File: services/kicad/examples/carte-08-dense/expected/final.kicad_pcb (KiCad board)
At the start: 2 copper layers, 57.3 x 44 mm, 56 parts, among them J1 IN_5V, J10 IO0, J11 IO1, J12 IO2, J13 IO3, J14 IO4, J2 SWD, U1 STM32F103C8T6, U2 AMS1117-3.3

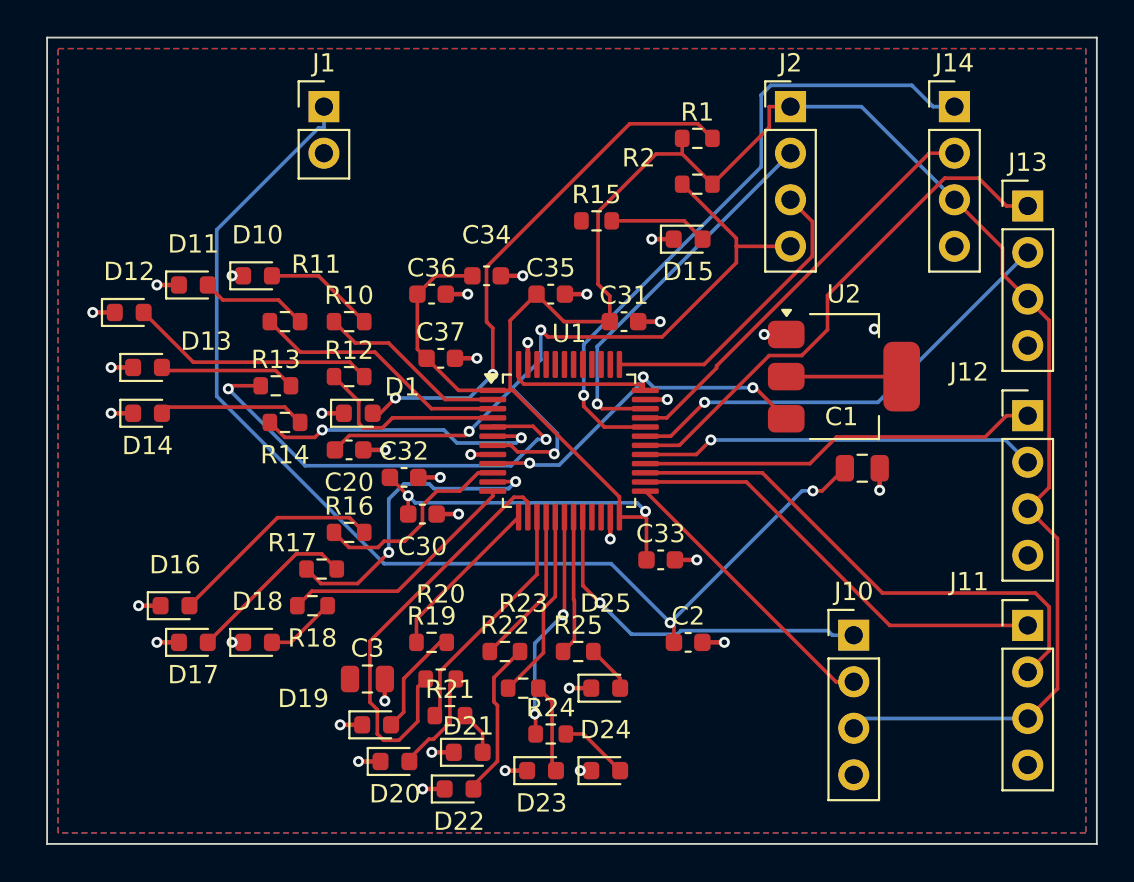
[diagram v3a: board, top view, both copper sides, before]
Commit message: fix(banc): le banc route comme la production — plafond 8, budget du client
D-2026-09-24-f. run_pipeline.py prenait 2 couches et 1800 s par défaut, et
carte-07 écrivait 2 en dur : dix cartes sur quinze ne pouvaient jamais
escalader, et la règle « toute connexion manquante fait monter » était
inerte dans le banc. Mesuré sur carte-07 : 97 %, seule la masse manquante,
« le palier suivant sera tenté »… puis retour à 2 couches.

Plafond par défaut 8 (client Pro Max), budget min(600 + 300 x plafond, 3600)
comme routingSearchBudgetS côté client. En production, rien ne change : le
plafond reste celui du plan.

Livraisons du jour, toutes vérifiées par kicad-cli et contre le schéma
(0 erreur bloquante, 0 connexion manquante, 0 court-circuit) :
carte-04, 05, 06, 08 (campagne de l'après-midi) et carte-09, 10 (4 couches).
Les boards versionnés de ces cartes court-circuitaient des nets du schéma.

Correction de ma propre erreur dans la doc : carte-07 n'avait jamais
escaladé ; les lignes « palier 4 et 6 » du journal étaient celles de
carte-08, démarrée la même minute.

Co-Authored-By: Claude Opus 5.5 <noreply@anthropic.com>
Claude-Session: https://claude.ai/code/session_01TnMqm4La2CxQHHB5K8aSSV
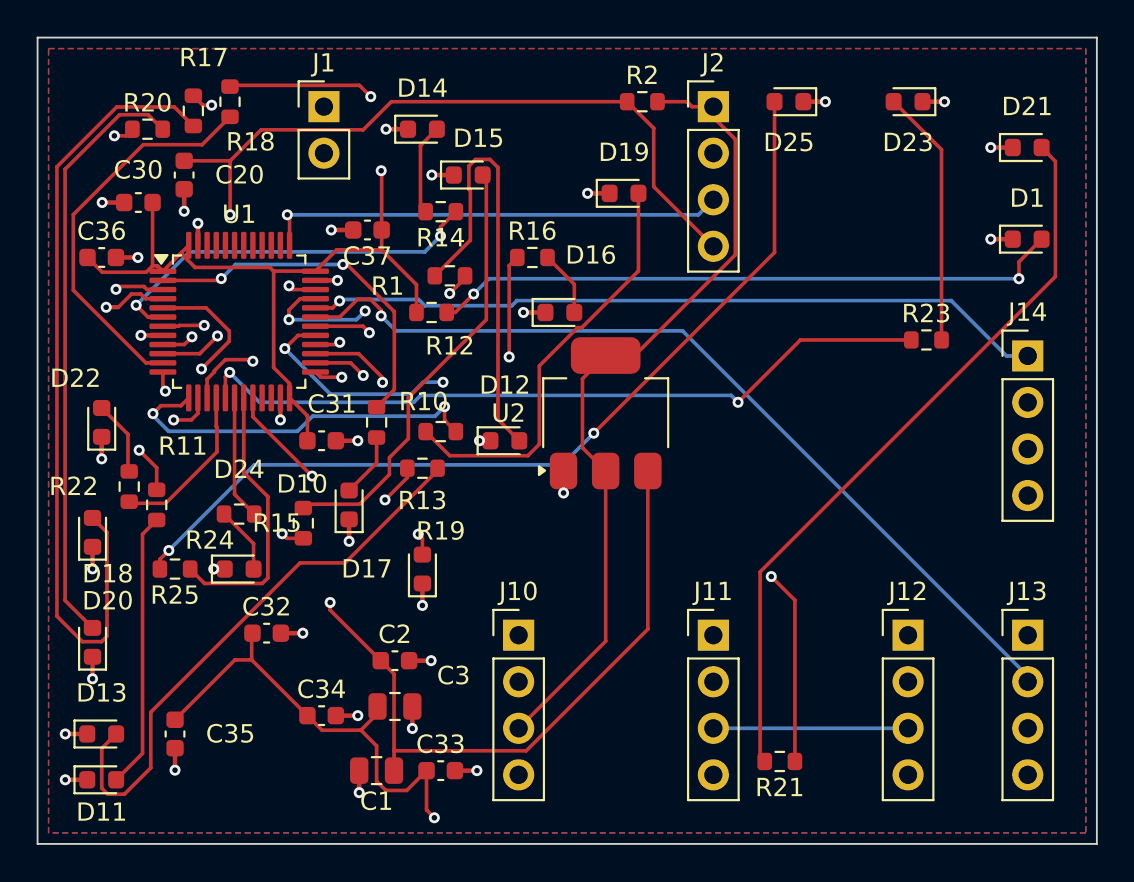
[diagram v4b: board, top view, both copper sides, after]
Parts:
- moved D21 44.9 mm to (140.0, 63.5)
- moved D23 41.6 mm to (133.5, 61.0), turned to 180 degrees
- moved D1 37.7 mm to (140.0, 68.5)
- moved R20 34.0 mm to (92.0, 62.5)
- moved D25 33.5 mm to (127.0, 61.0), turned to 180 degrees
- moved D19 32.0 mm to (118.0, 66.0)
- moved C35 31.6 mm to (93.5, 95.5), turned to -90 degrees
- moved C1 31.2 mm to (104.5, 97.5), turned to 180 degrees
- moved R23 29.1 mm to (134.5, 74.0)
- moved D22 27.9 mm to (89.5, 78.5), turned to 90 degrees
- moved R18 27.8 mm to (94.5, 61.5), turned to -90 degrees
- moved D11 27.5 mm to (89.5, 98.0)
- moved D16 26.4 mm to (114.5, 72.5)
- moved R17 26.0 mm to (96.5, 61.0), turned to 90 degrees
- moved C34 25.6 mm to (101.5, 94.5)
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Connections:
- C3 pad 1: Net-(C3-1) -> +3V3
- U1 pad 36: PWR_FLAG -> +3V3
- U1 pad 48: PWR_FLAG -> +3V3
- U1 pad 9: PWR_FLAG -> IO_L5
- U2 pad 2: Net-(U2-2) -> +3V3
- U2 pad 3: PWR_FLAG -> VIN
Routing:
- net +3V3: track 127.2 -> 181.6 mm
- net LEDA15: track 2.61 -> 49.2 mm, vias 0 -> 2
- net LEDA8: track 3.87 -> 44.0 mm
- net LEDA11: track 2.40 -> 40.6 mm
- net IO_L11: track 13.1 -> 48.0 mm, vias 0 -> 2
- net IO_L13: track 10.4 -> 41.1 mm, vias 0 -> 2
- net PWR_FLAG: track 27.8 -> 0.00 mm, vias 3 -> 0
- net LEDA10: track 5.70 -> 32.5 mm
- net LEDA7: track 9.38 -> 34.5 mm, vias 0 -> 2
- net LEDA3: track 7.45 -> 31.0 mm
- net EXT3_2: track 25.0 -> 48.3 mm
- net EXT2_2: track 21.7 -> 44.0 mm, vias 1 -> 2
- net EXT4_2: track 22.9 -> 45.1 mm, vias 0 -> 2
- net LEDA5: track 5.38 -> 24.1 mm
- net EXT3_1: track 28.6 -> 45.9 mm, vias 0 -> 1
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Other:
- board size 57.3 x 44 mm -> 57.8 x 44 mm
- copper layers 2 -> 4
